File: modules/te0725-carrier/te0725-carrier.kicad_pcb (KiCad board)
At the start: 2 copper layers, 42 x 132.1 mm, 3 parts, among them J1 Conn_02x25_Odd_Even, J2 Conn_02x25_Odd_Even

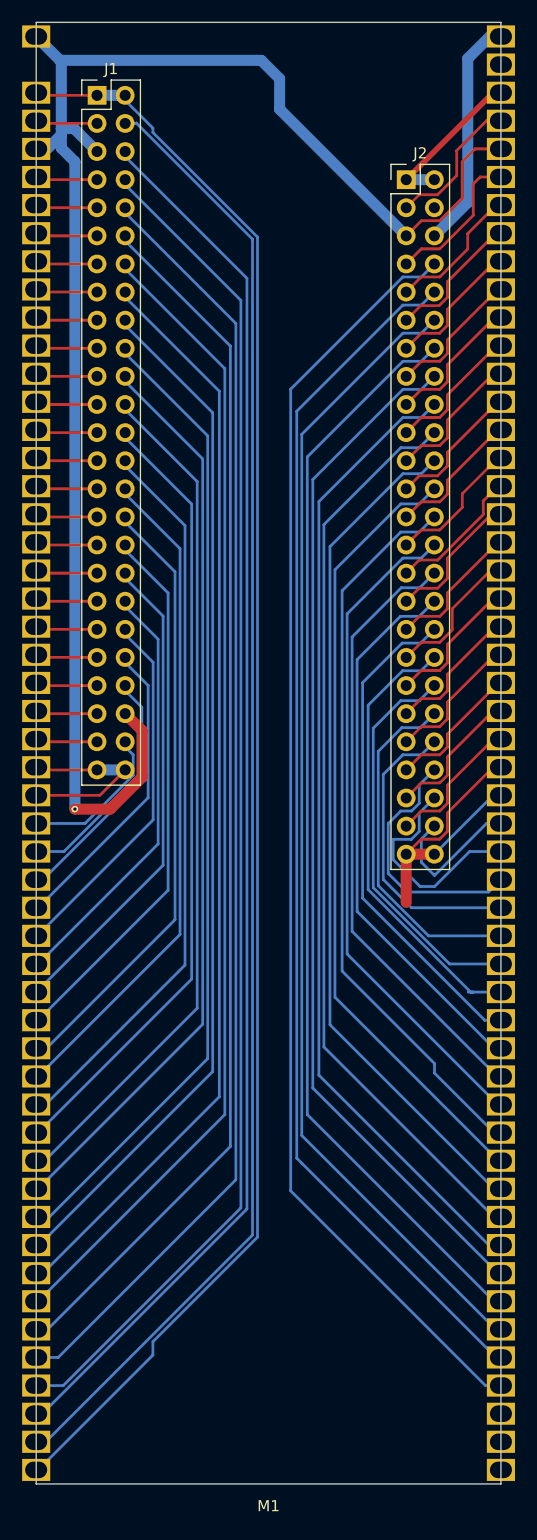
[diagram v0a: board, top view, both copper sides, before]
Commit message: finish te0725 carrier module layout
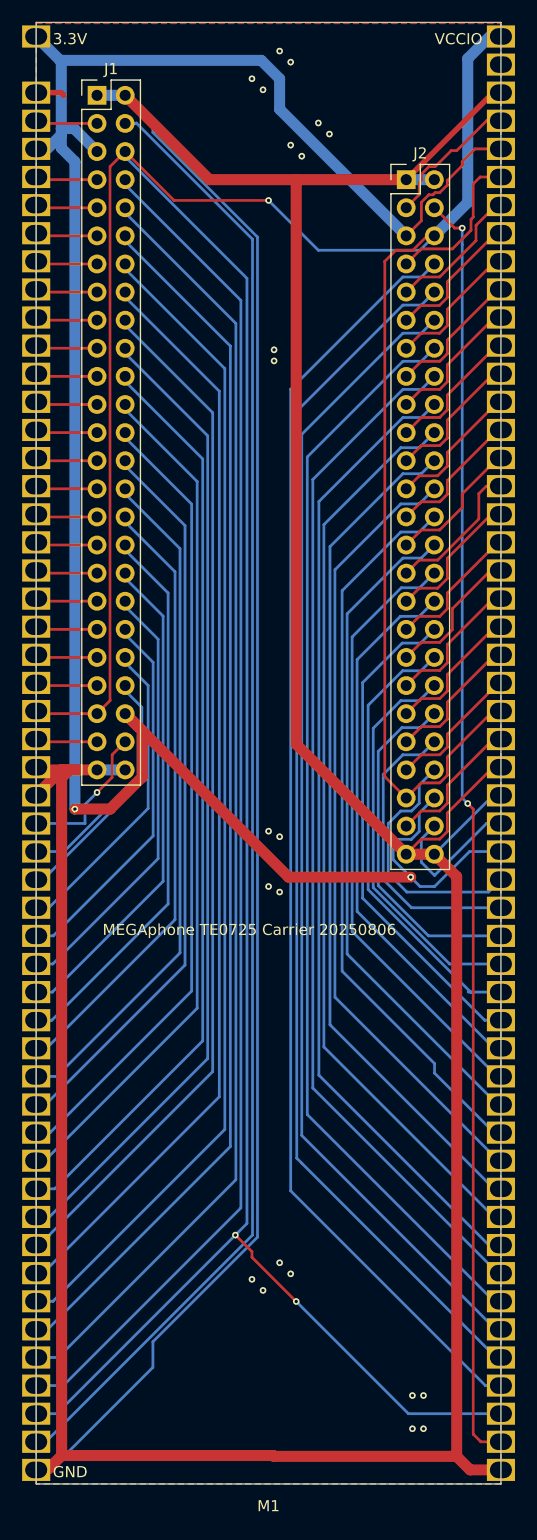
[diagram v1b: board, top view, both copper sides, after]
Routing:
- net J1_1: track 204.4 -> 444.7 mm, vias 0 -> 22
- net J1_45: track 166.1 -> 336.6 mm, vias 0 -> 3
- net J2_4: track 0.00 -> 115.5 mm, vias 0 -> 2
- net J1_46: track 183.4 -> 214.8 mm, vias 1 -> 2
- net J1_30: track 60.7 -> 61.6 mm
- net J1_22: track 82.7 -> 83.6 mm
- net J1_36: track 44.7 -> 45.5 mm
- net J1_40: track 33.8 -> 34.7 mm
- net J1_14: track 104.6 -> 105.4 mm
- net J1_48: track 14.5 -> 13.7 mm, vias 0 -> 1
- net J1_38: track 39.3 -> 40.1 mm
- net J1_34: track 50.2 -> 51.0 mm
- net J2_7: track 13.5 -> 14.2 mm
- net J1_26: track 71.7 -> 72.3 mm
- net J2_29: track 12.5 -> 13.2 mm
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- added copper zone on B.Cu, net J1_1
- added copper zone on F.Cu, net J1_1
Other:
- board text added: "3.3V"
- board text added: "GND"
- board text added: "MEGAphone TE0725 Carrier 20250806"
- board text added: "VCCIO"
